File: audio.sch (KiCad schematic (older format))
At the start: 1 part

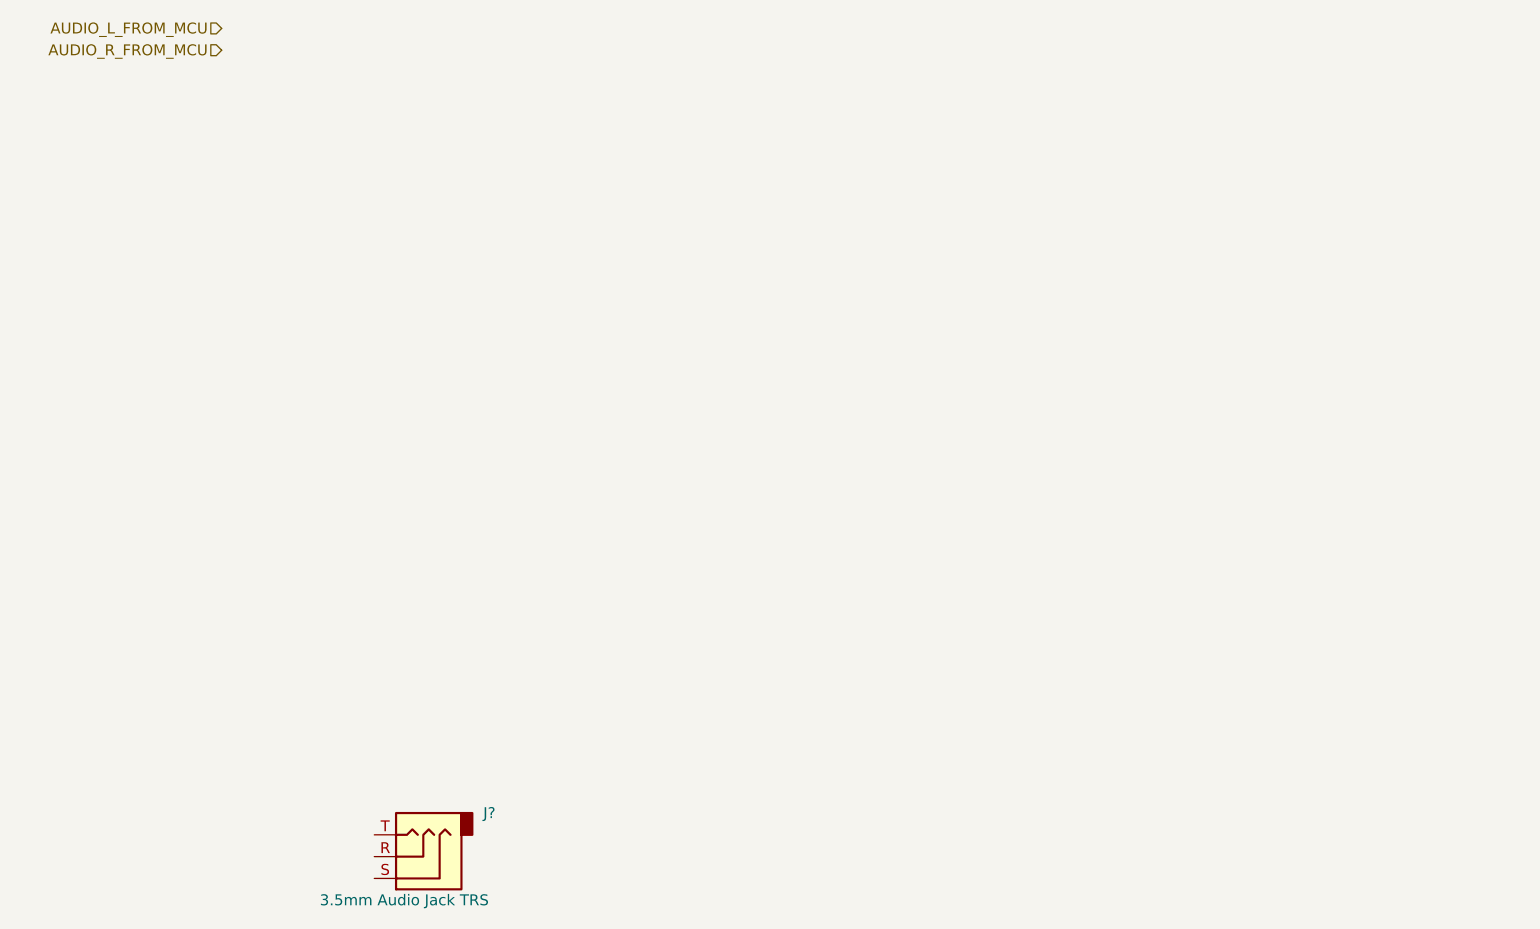
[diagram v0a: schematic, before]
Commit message: Added some footprints. Basic board outline.
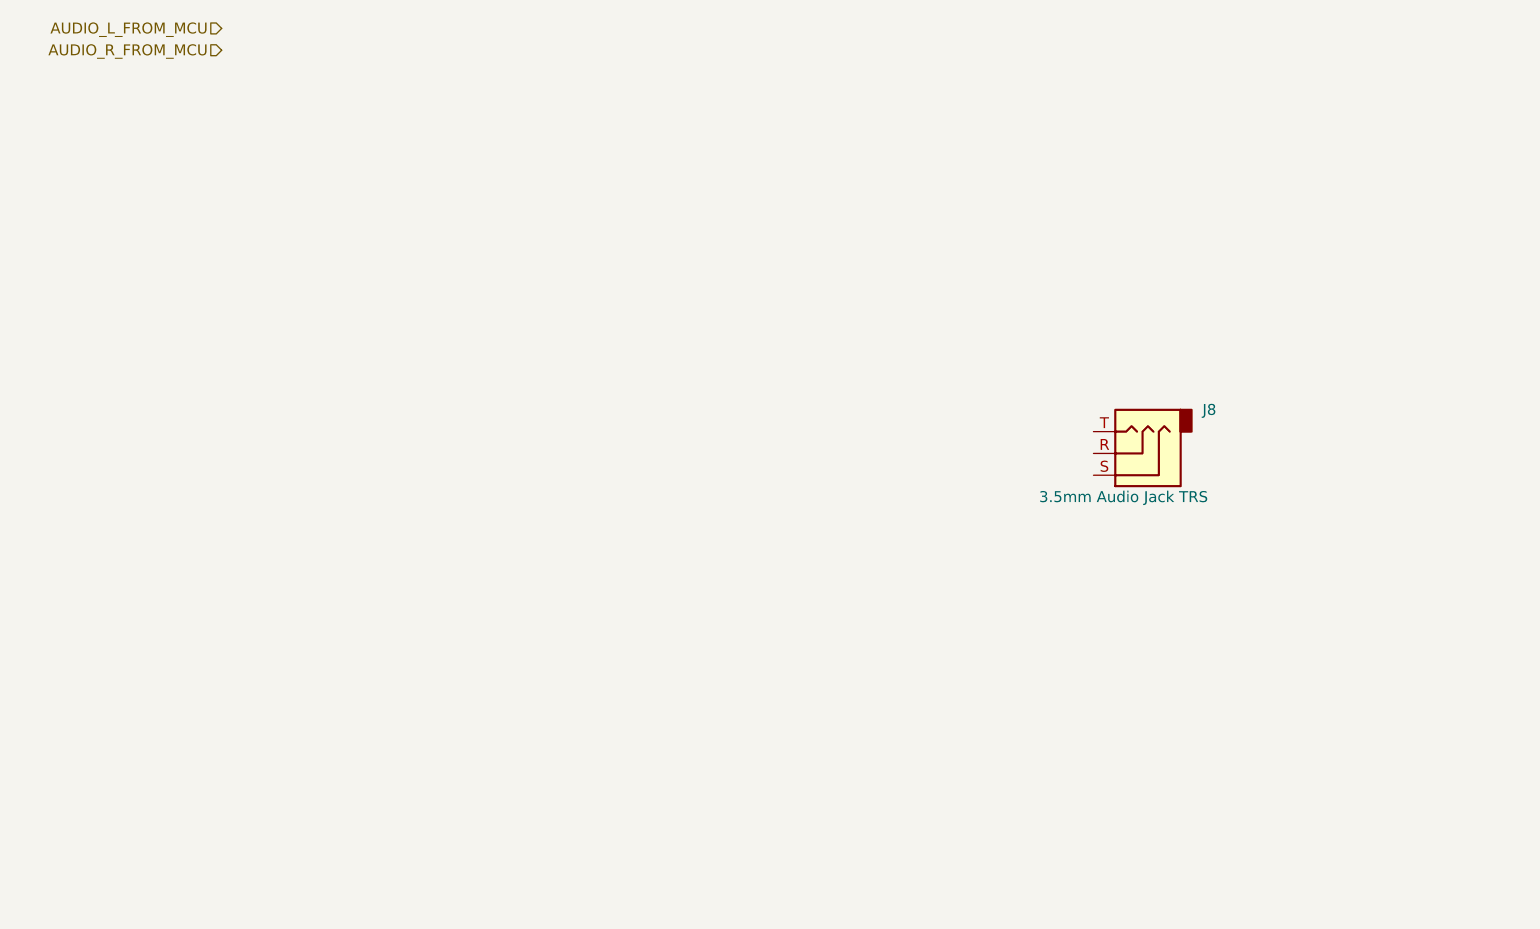
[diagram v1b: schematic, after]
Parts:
- J8: renamed from J?; footprint (none) -> Connector_Audio:Jack_3.5mm_CUI_SJ1-3533NG_Horizontal
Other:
- moved on the sheet: J8
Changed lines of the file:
@@
 $Descr A4 11693 8268
 encoding utf-8
-Sheet 8 11
+Sheet 4 11
 Title "Neotron 32K"
 Date "2019-12-08"
@@
 L Connector:AudioJack3 J?
 U 1 1 5DF41F43
-P 2600 5200
+P 5900 3350
 AR Path="/5DF41F43" Ref="J?"  Part="1"
-AR Path="/5DF3EA3F/5DF41F43" Ref="J?"  Part="1"
-F 0 "J?" H 2300 5000 50  0000 R CNN
-F 1 "3.5mm Audio Jack TRS" H 3050 5400 50  0000 R CNN
-F 2 "" H 2600 5200 50  0001 C CNN
-F 3 "~" H 2600 5200 50  0001 C CNN
-	1    2600 5200
+AR Path="/5DF3EA3F/5DF41F43" Ref="J8"  Part="1"
+F 0 "J8" H 5600 3150 50  0000 R CNN
+F 1 "3.5mm Audio Jack TRS" H 6350 3550 50  0000 R CNN
+F 2 "Connector_Audio:Jack_3.5mm_CUI_SJ1-3533NG_Horizontal" H 5900 3350 50  0001 C CNN
+F 3 "~" H 5900 3350 50  0001 C CNN
+	1    5900 3350
 	-1   0    0    1
 $EndComp

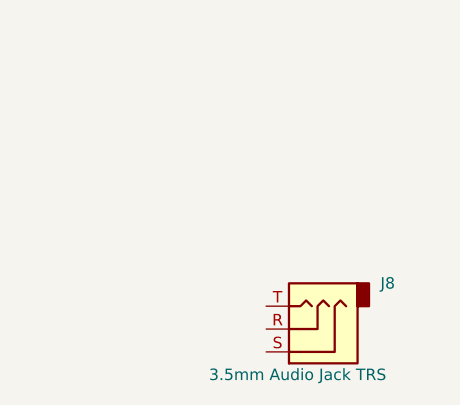
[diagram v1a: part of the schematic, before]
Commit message: Completed Power, SD, MIDI, Parallel and Joystick sheets.
Switch to sheet based 100x part numbering.
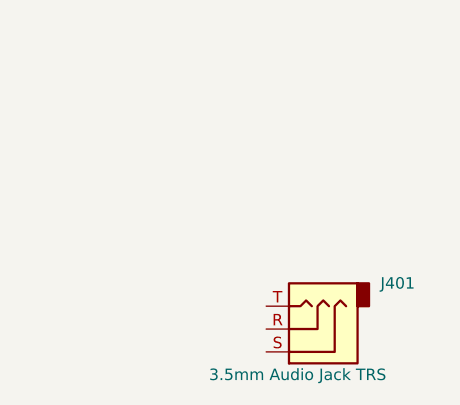
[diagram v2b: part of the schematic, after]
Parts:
- renumbered J8 to J401
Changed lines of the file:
@@
 P 5900 3350
 AR Path="/5DF41F43" Ref="J?"  Part="1"
-AR Path="/5DF3EA3F/5DF41F43" Ref="J8"  Part="1"
-F 0 "J8" H 5600 3150 50  0000 R CNN
+AR Path="/5DF3EA3F/5DF41F43" Ref="J401"  Part="1"
+F 0 "J401" H 5600 3150 50  0000 R CNN
 F 1 "3.5mm Audio Jack TRS" H 6350 3550 50  0000 R CNN
 F 2 "Connector_Audio:Jack_3.5mm_CUI_SJ1-3533NG_Horizontal" H 5900 3350 50  0001 C CNN

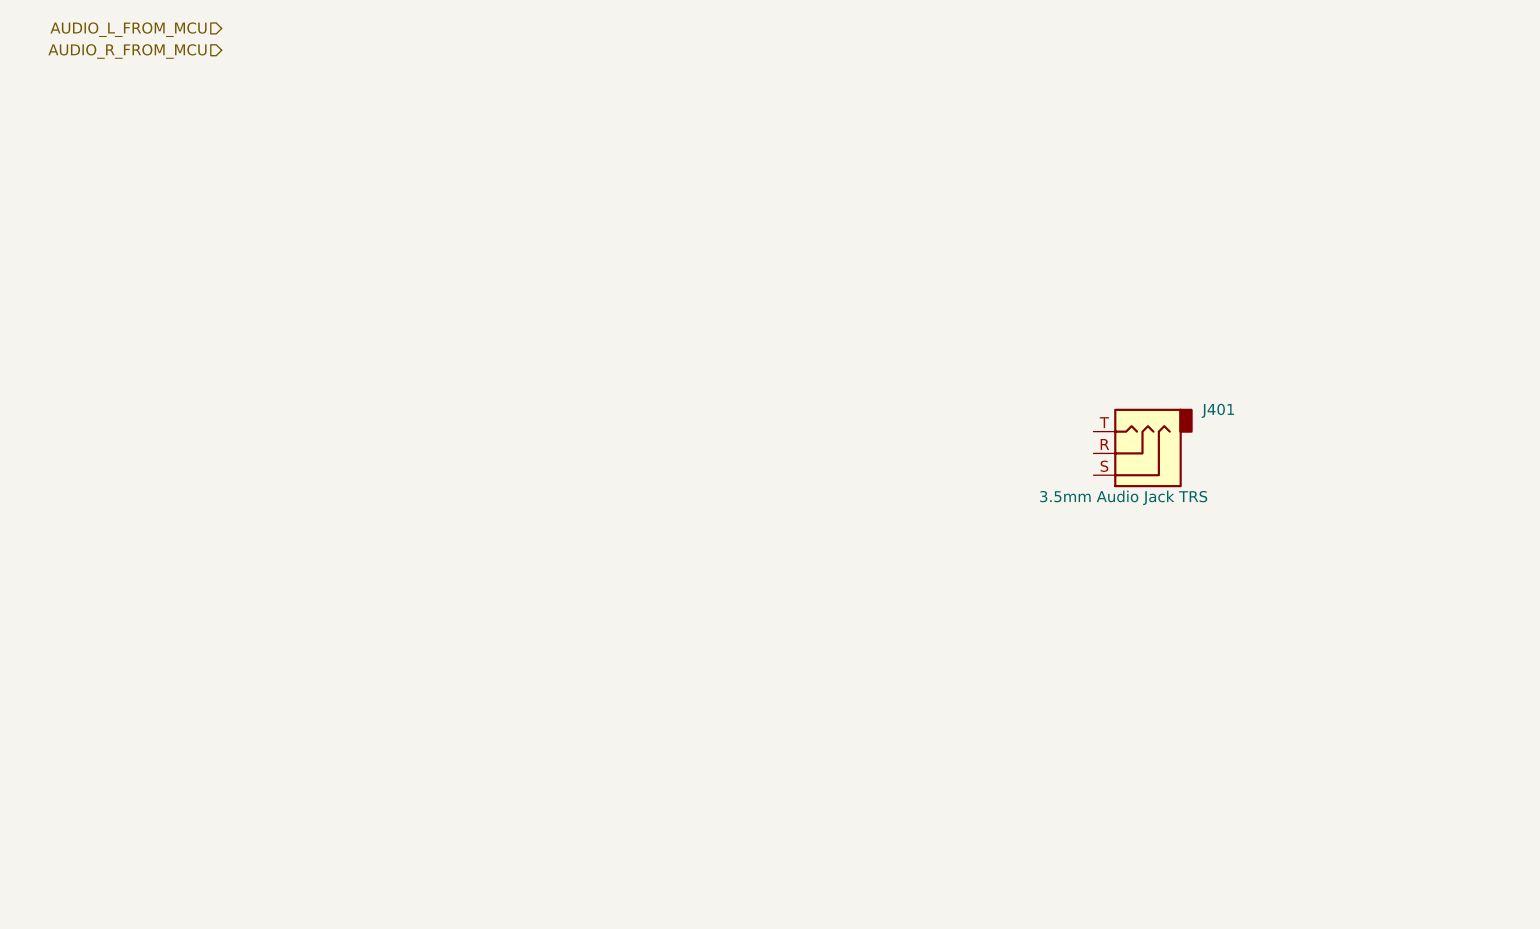
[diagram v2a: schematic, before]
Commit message: Schematic capture draft complete.
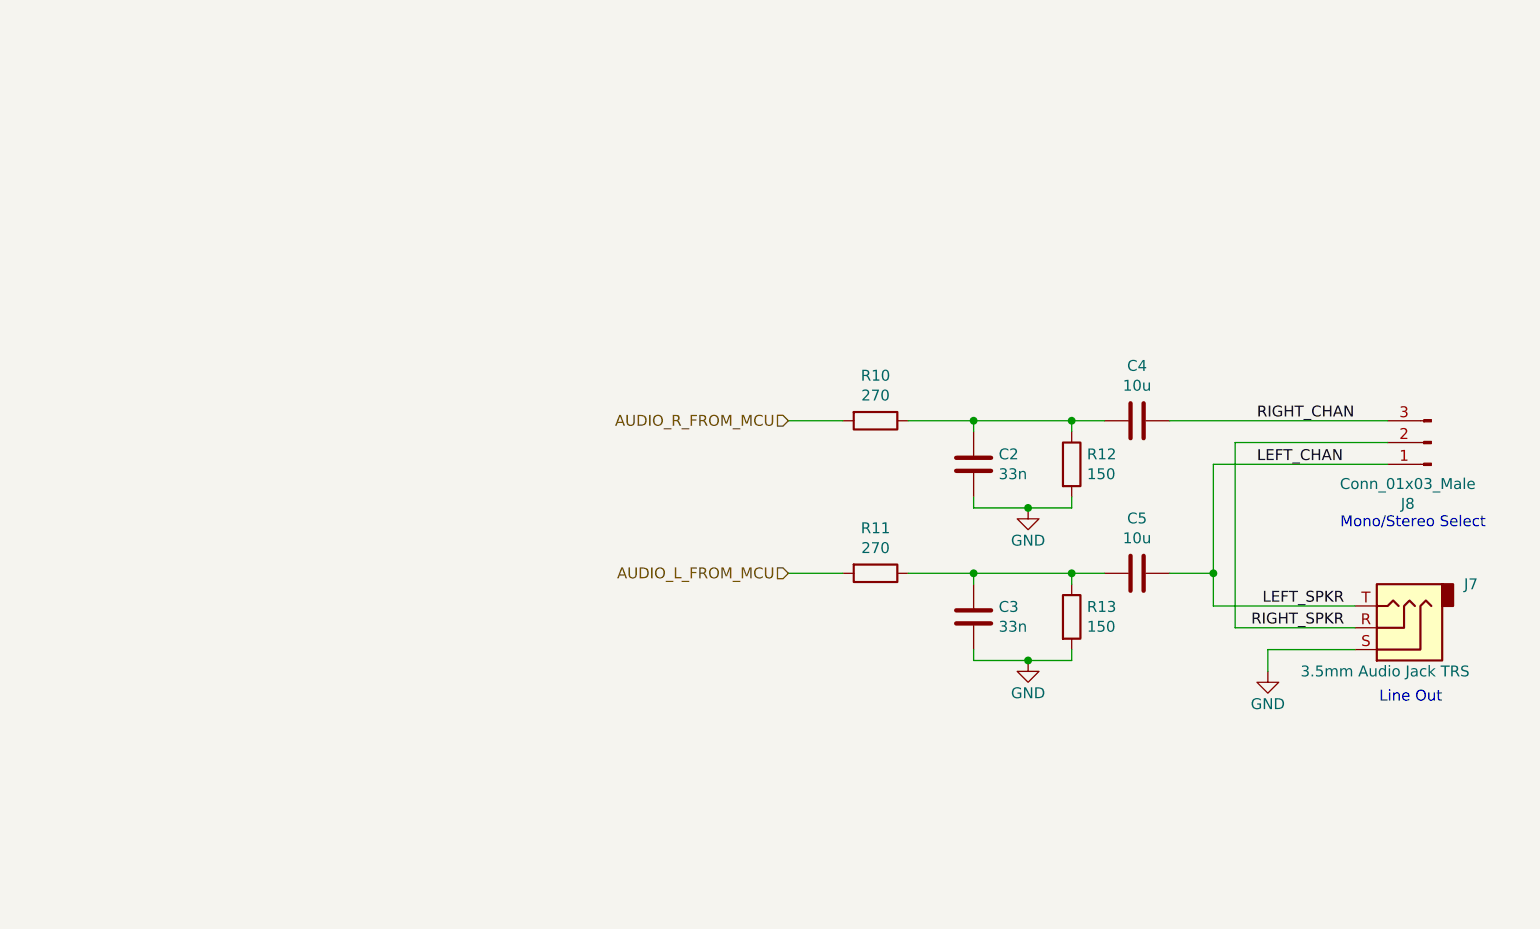
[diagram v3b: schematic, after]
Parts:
- added C2, C3: 33n, symbol Device:C
- added C4, C5: 10u, symbol Device:C
- added J8: Conn_01x03_Male, symbol Connector:Conn_01x03_Male
- added R10, R11: 270, symbol Device:R
- added R12, R13: 150, symbol Device:R
- renumbered J401 to J7
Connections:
- net AUDIO_L_FROM_MCU: now also R11.2
- net AUDIO_R_FROM_MCU: now also R10.2
- net RIGHT_SPKR: now reaches J7.R
- net RIGHT_SPKR: now also J8.2 (Pin_2)
- net GND: now reaches J7.S
- net GND: now also C2.1, C3.1, R12.2, R13.2
- net LEFT_CHAN: now reaches J7.T
- net LEFT_CHAN: now also C5.2, J8.1 (Pin_1)
- new net: C2.2, C4.1, R10.1, R12.1
- new net: C3.2, C5.1, R11.1, R13.1
- new net RIGHT_CHAN: C4.2, J8.3 (Pin_3)
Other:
- note added: "Line Out"
- note added: "Mono/Stereo Select"
- moved on the sheet: J7

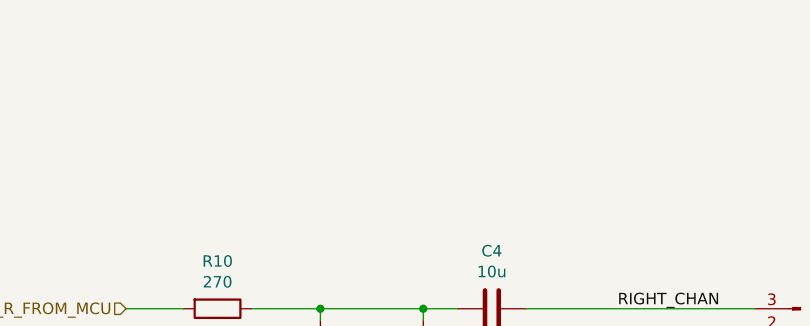
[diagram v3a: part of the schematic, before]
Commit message: Tidied up Atmega power. Added page titles.
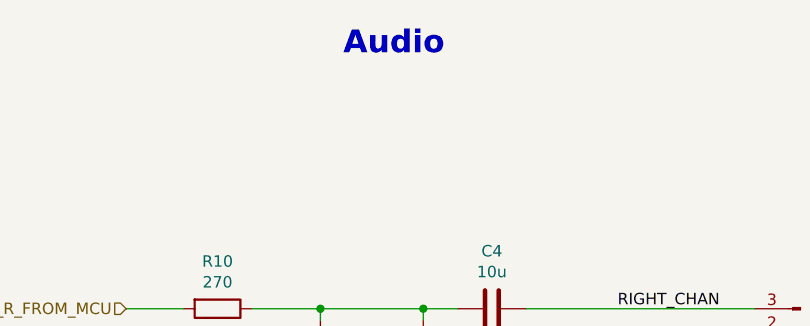
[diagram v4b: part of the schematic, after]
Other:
- note added: "Audio"
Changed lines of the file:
@@
 Sheet 3 10
 Title "Neotron 32K Main PCB"
-Date "2019-12-15"
-Rev "0.5"
+Date "2019-12-16"
+Rev "0.6"
 Comp "github.com/neotron-compute/Neotron-32-Hardware"
 Comment1 "Copyright (c) Jonathan 'theJPster' Pallant"
@@
 Wire Wire Line
 	6350 3300 6350 4150
+Text Notes 5250 2100 0    100  ~ 20
+Audio
 $EndSCHEMATC

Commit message: Work in progress.
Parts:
- C2, C3, C4, C5: footprint (none) -> Capacitor_THT:C_Disc_D3.0mm_W2.0mm_P2.50mm
- J8: footprint (none) -> Connector_PinHeader_2.54mm:PinHeader_1x03_P2.54mm_Vertical
- R10, R11, R12, R13: footprint (none) -> Resistor_THT:R_Axial_DIN0411_L9.9mm_D3.6mm_P12.70mm_Horizontal
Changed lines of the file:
@@
 F 0 "J8" H 7358 3581 50  0000 C CNN
 F 1 "Conn_01x03_Male" H 7358 3490 50  0000 C CNN
-F 2 "" H 7250 3300 50  0001 C CNN
+F 2 "Connector_PinHeader_2.54mm:PinHeader_1x03_P2.54mm_Vertical" H 7250 3300 50  0001 C CNN
 F 3 "~" H 7250 3300 50  0001 C CNN
 	1    7250 3300
@@
 F 0 "C4" V 6152 3200 50  0000 C CNN
 F 1 "10u" V 6061 3200 50  0000 C CNN
-F 2 "" H 5938 3050 50  0001 C CNN
+F 2 "Capacitor_THT:C_Disc_D3.0mm_W2.0mm_P2.50mm" H 5938 3050 50  0001 C CNN
 F 3 "~" H 5900 3200 50  0001 C CNN
 	1    5900 3200
@@
 F 0 "C5" V 6152 3900 50  0000 C CNN
 F 1 "10u" V 6061 3900 50  0000 C CNN
-F 2 "" H 5938 3750 50  0001 C CNN
+F 2 "Capacitor_THT:C_Disc_D3.0mm_W2.0mm_P2.50mm" H 5938 3750 50  0001 C CNN
 F 3 "~" H 5900 3900 50  0001 C CNN
 	1    5900 3900
@@
 F 0 "R12" H 5670 3446 50  0000 L CNN
 F 1 "150" H 5670 3355 50  0000 L CNN
-F 2 "" V 5530 3400 50  0001 C CNN
+F 2 "Resistor_THT:R_Axial_DIN0411_L9.9mm_D3.6mm_P12.70mm_Horizontal" V 5530 3400 50  0001 C CNN
 F 3 "~" H 5600 3400 50  0001 C CNN
 	1    5600 3400
@@
 F 0 "R13" H 5670 4146 50  0000 L CNN
 F 1 "150" H 5670 4055 50  0000 L CNN
-F 2 "" V 5530 4100 50  0001 C CNN
+F 2 "Resistor_THT:R_Axial_DIN0411_L9.9mm_D3.6mm_P12.70mm_Horizontal" V 5530 4100 50  0001 C CNN
 F 3 "~" H 5600 4100 50  0001 C CNN
 	1    5600 4100
@@
 F 0 "R11" V 4493 3900 50  0000 C CNN
 F 1 "270" V 4584 3900 50  0000 C CNN
-F 2 "" V 4630 3900 50  0001 C CNN
+F 2 "Resistor_THT:R_Axial_DIN0411_L9.9mm_D3.6mm_P12.70mm_Horizontal" V 4630 3900 50  0001 C CNN
 F 3 "~" H 4700 3900 50  0001 C CNN
 	1    4700 3900
@@
 F 0 "R10" V 4493 3200 50  0000 C CNN
 F 1 "270" V 4584 3200 50  0000 C CNN
-F 2 "" V 4630 3200 50  0001 C CNN
+F 2 "Resistor_THT:R_Axial_DIN0411_L9.9mm_D3.6mm_P12.70mm_Horizontal" V 4630 3200 50  0001 C CNN
 F 3 "~" H 4700 3200 50  0001 C CNN
 	1    4700 3200
@@
 F 0 "C3" H 5035 4054 50  0000 R CNN
 F 1 "33n" H 5035 4145 50  0000 R CNN
-F 2 "" H 5188 3950 50  0001 C CNN
+F 2 "Capacitor_THT:C_Disc_D3.0mm_W2.0mm_P2.50mm" H 5188 3950 50  0001 C CNN
 F 3 "~" H 5150 4100 50  0001 C CNN
 	1    5150 4100
@@
 F 0 "C2" H 5035 3354 50  0000 R CNN
 F 1 "33n" H 5035 3445 50  0000 R CNN
-F 2 "" H 5188 3250 50  0001 C CNN
+F 2 "Capacitor_THT:C_Disc_D3.0mm_W2.0mm_P2.50mm" H 5188 3250 50  0001 C CNN
 F 3 "~" H 5150 3400 50  0001 C CNN
 	1    5150 3400

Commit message: Updated footprints: ) Swapped RS-232 DE9 for IDC header. ) Large caps are radial electrolytics. ) Made resistors a little smaller.
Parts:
- C4, C5: footprint Capacitor_THT:C_Disc_D3.0mm_W2.0mm_P2.50mm -> Capacitor_THT:CP_Radial_D6.3mm_P2.50mm
- R10, R11, R12, R13: footprint Resistor_THT:R_Axial_DIN0411_L9.9mm_D3.6mm_P12.70mm_Horizontal -> Resistor_THT:R_Axial_DIN0207_L6.3mm_D2.5mm_P10.16mm_Horizontal
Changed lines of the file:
@@
 F 0 "C4" V 6152 3200 50  0000 C CNN
 F 1 "10u" V 6061 3200 50  0000 C CNN
-F 2 "Capacitor_THT:C_Disc_D3.0mm_W2.0mm_P2.50mm" H 5938 3050 50  0001 C CNN
+F 2 "Capacitor_THT:CP_Radial_D6.3mm_P2.50mm" H 5938 3050 50  0001 C CNN
 F 3 "~" H 5900 3200 50  0001 C CNN
 	1    5900 3200
@@
 F 0 "C5" V 6152 3900 50  0000 C CNN
 F 1 "10u" V 6061 3900 50  0000 C CNN
-F 2 "Capacitor_THT:C_Disc_D3.0mm_W2.0mm_P2.50mm" H 5938 3750 50  0001 C CNN
+F 2 "Capacitor_THT:CP_Radial_D6.3mm_P2.50mm" H 5938 3750 50  0001 C CNN
 F 3 "~" H 5900 3900 50  0001 C CNN
 	1    5900 3900
@@
 F 0 "R12" H 5670 3446 50  0000 L CNN
 F 1 "150" H 5670 3355 50  0000 L CNN
-F 2 "Resistor_THT:R_Axial_DIN0411_L9.9mm_D3.6mm_P12.70mm_Horizontal" V 5530 3400 50  0001 C CNN
+F 2 "Resistor_THT:R_Axial_DIN0207_L6.3mm_D2.5mm_P10.16mm_Horizontal" V 5530 3400 50  0001 C CNN
 F 3 "~" H 5600 3400 50  0001 C CNN
 	1    5600 3400
@@
 F 0 "R13" H 5670 4146 50  0000 L CNN
 F 1 "150" H 5670 4055 50  0000 L CNN
-F 2 "Resistor_THT:R_Axial_DIN0411_L9.9mm_D3.6mm_P12.70mm_Horizontal" V 5530 4100 50  0001 C CNN
+F 2 "Resistor_THT:R_Axial_DIN0207_L6.3mm_D2.5mm_P10.16mm_Horizontal" V 5530 4100 50  0001 C CNN
 F 3 "~" H 5600 4100 50  0001 C CNN
 	1    5600 4100
@@
 F 0 "R11" V 4493 3900 50  0000 C CNN
 F 1 "270" V 4584 3900 50  0000 C CNN
-F 2 "Resistor_THT:R_Axial_DIN0411_L9.9mm_D3.6mm_P12.70mm_Horizontal" V 4630 3900 50  0001 C CNN
+F 2 "Resistor_THT:R_Axial_DIN0207_L6.3mm_D2.5mm_P10.16mm_Horizontal" V 4630 3900 50  0001 C CNN
 F 3 "~" H 4700 3900 50  0001 C CNN
 	1    4700 3900
@@
 F 0 "R10" V 4493 3200 50  0000 C CNN
 F 1 "270" V 4584 3200 50  0000 C CNN
-F 2 "Resistor_THT:R_Axial_DIN0411_L9.9mm_D3.6mm_P12.70mm_Horizontal" V 4630 3200 50  0001 C CNN
+F 2 "Resistor_THT:R_Axial_DIN0207_L6.3mm_D2.5mm_P10.16mm_Horizontal" V 4630 3200 50  0001 C CNN
 F 3 "~" H 4700 3200 50  0001 C CNN
 	1    4700 3200
